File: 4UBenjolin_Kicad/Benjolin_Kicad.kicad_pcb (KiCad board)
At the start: 2 copper layers, 254 x 177.8 mm, 144 parts, among them J1 Conn_01x04_Male, J10 MAINOUT, J11 PWM, J12 RUN, J13 XOR, J14 CV_1, J15 CV_2, J16 Mix_In_3, J17 Mix_In_4, J18 Mixer_Out, J2 Mix_In_1, J3 Mix_In_2, J4 EXT.INPUT, J5 CV_F, J6 PUL2, J7 TRI1, J8 TRI2, J9 PUL1, Q1 BC547, SW1 SW_SPDT, U1 TL074, U2 TL072, U3 TL074, U4 TL074, U5 SSI2164, U6 4021, U7 L78L09_SOT89, U8 79L09, U9 TL071

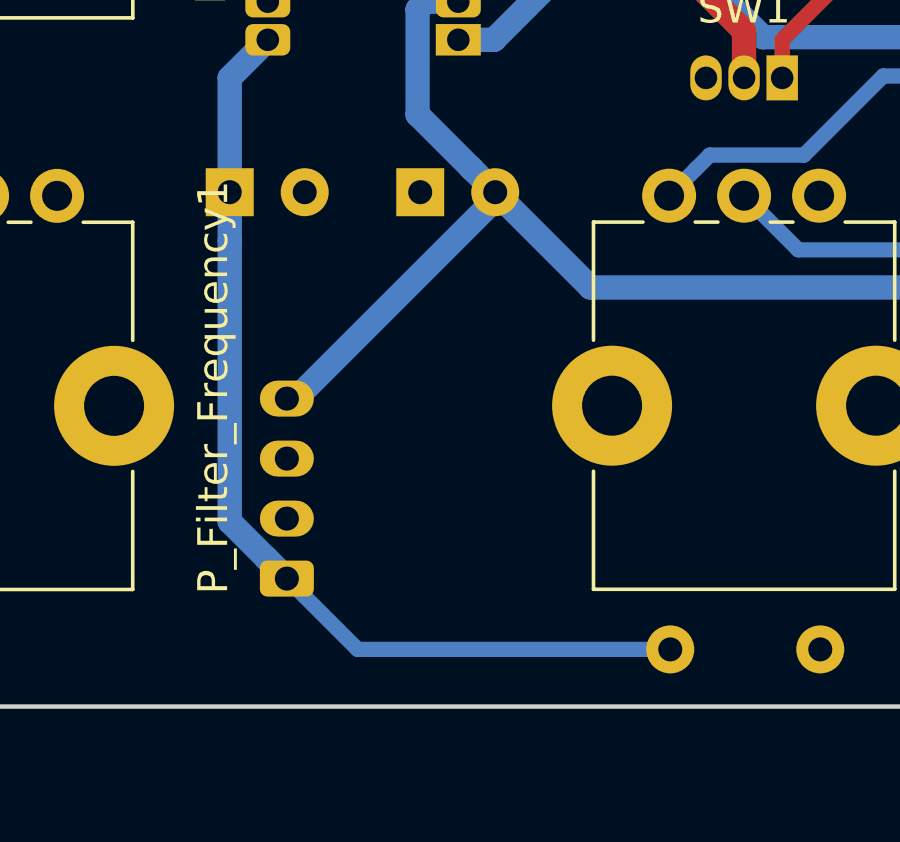
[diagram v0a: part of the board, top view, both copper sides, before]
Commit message: pots are off center still and need to connect one of the ground pins
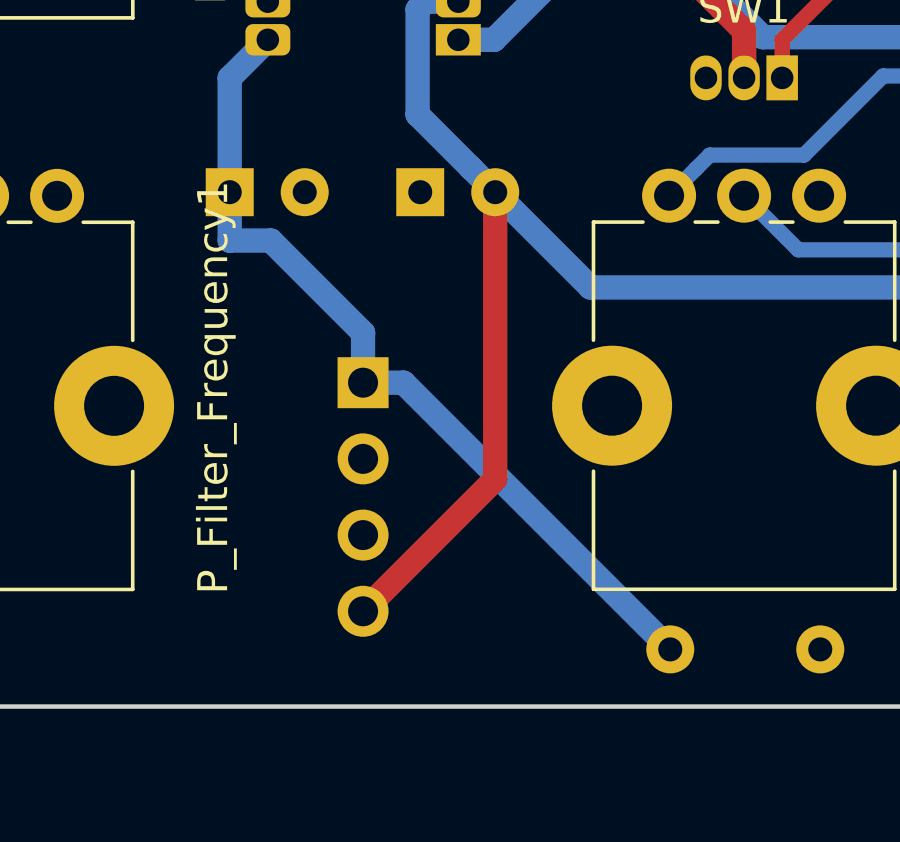
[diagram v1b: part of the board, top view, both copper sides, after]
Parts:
- J1: footprint Connector_Molex:Molex_Micro-Latch_53254-0470_1x04_P2.00mm_Horizontal -> Connector_PinHeader_2.54mm:PinHeader_1x04_P2.54mm_Vertical
- moved J1 7.01 mm to (254.0, 154.3), turned to 180 degrees
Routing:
- net -12V: track 37.7 -> 43.8 mm
- net +12V: track 33.0 -> 28.5 mm
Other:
- board text added: "Version 1"

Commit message: made separate panel
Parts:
- moved REF** 41.9 mm to (134.0, 71.4)
- moved REF** 41.9 mm to (134.0, 52.4)
- moved REF** 41.9 mm to (134.0, 90.5)
- moved REF** 41.9 mm to (134.0, 109.5)
- moved REF** 41.9 mm to (83.2, 52.4)
- moved REF** 41.9 mm to (83.2, 71.4)
- moved REF** 41.9 mm to (83.2, 90.5)
- moved REF** 41.9 mm to (83.2, 109.5)
- moved REF** 41.9 mm to (159.4, 52.4)
- moved REF** 41.9 mm to (159.4, 33.3)
- moved REF** 41.9 mm to (159.4, 71.4)
- moved REF** 41.9 mm to (108.6, 90.5)
- moved REF** 41.9 mm to (108.6, 71.4)
- moved REF** 41.9 mm to (108.6, 52.4)
- moved REF** 41.9 mm to (108.6, 109.5)
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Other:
- board size 254 x 177.8 mm -> 212.1 x 177.8 mm

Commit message: Built Gerbers
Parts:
- removed REF** (x17): Banana Jack, SynthComponents:Banana _Jack_Panel
- turned P_Chan1 to 270 degrees
- turned P_Chan2 to 270 degrees
- turned P_Chan3 to 270 degrees
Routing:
- net GND: track 22.3 -> 84.8 mm, vias 130 -> 146
- net Net-(J2-Pad1): track 18.7 -> 35.7 mm, vias 0 -> 1
- net Net-(J16-Pad1): track 20.6 -> 37.2 mm
- net Net-(P_Chan2-Pad2): track 10.3 -> 23.2 mm
- net Net-(P_Chan1-Pad2): track 36.8 -> 48.0 mm
- net Net-(P_Chan3-Pad2): track 9.63 -> 20.7 mm
- net Net-(J3-Pad1): track 26.8 -> 37.3 mm
- net FCV: track 34.9 -> 44.2 mm
- net Net-(C5-Pad1): track 186.2 -> 178.5 mm
- net V+: track 374.2 -> 370.3 mm, vias 10 -> 12
- net Net-(C19-Pad1): track 34.6 -> 36.3 mm
- net VCA1Out: track 84.3 -> 85.9 mm
- net Net-(J18-Pad1): track 41.8 -> 43.3 mm
- net RUN_CV: track 214.9 -> 213.4 mm, vias 7 -> 8
- net (no net): vias 2 -> 0
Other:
- board size 212.1 x 177.8 mm -> 101.6 x 152.4 mm
- board text removed: "4mm hole"
- board text removed: "BENJOLIN AND MIXER"
- board text removed: "CV"
- board text removed: "EXT. IN"
- board text removed: "FILTER FREQ"
- board text removed: "FREQ A"
- board text removed: "FREQ B"
- board text removed: "IN 1"
- board text removed: "IN 2"
- board text removed: "IN 3"
- board text removed: "IN 4"
- board text removed: "LOOP I/Ø"
- board text removed: "LOOP OFFSET"
- board text removed: "MAIN OUT"
- board text removed: "MIX OUT"
- board text removed: "PULSE"
- board text removed: "PWM"
- board text removed: "RESONANCE"
- board text removed: "RUNGLER"
- board text removed: "RUNGLER CV"
- board text removed: "TRIANGLE"
- board text removed: "XOR"

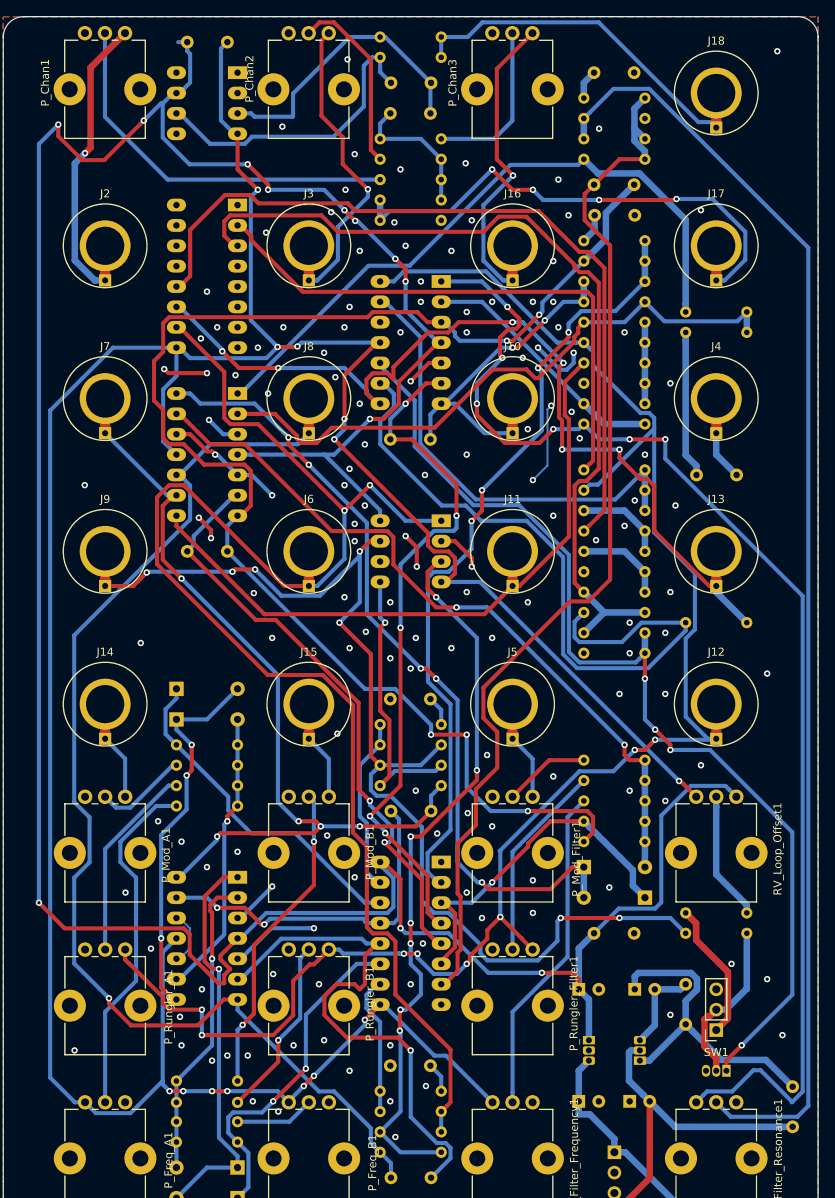
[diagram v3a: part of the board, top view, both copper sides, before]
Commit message: All bugs fixed. -v rail, flipped pots, power to 4021, tl071 opamp flipped
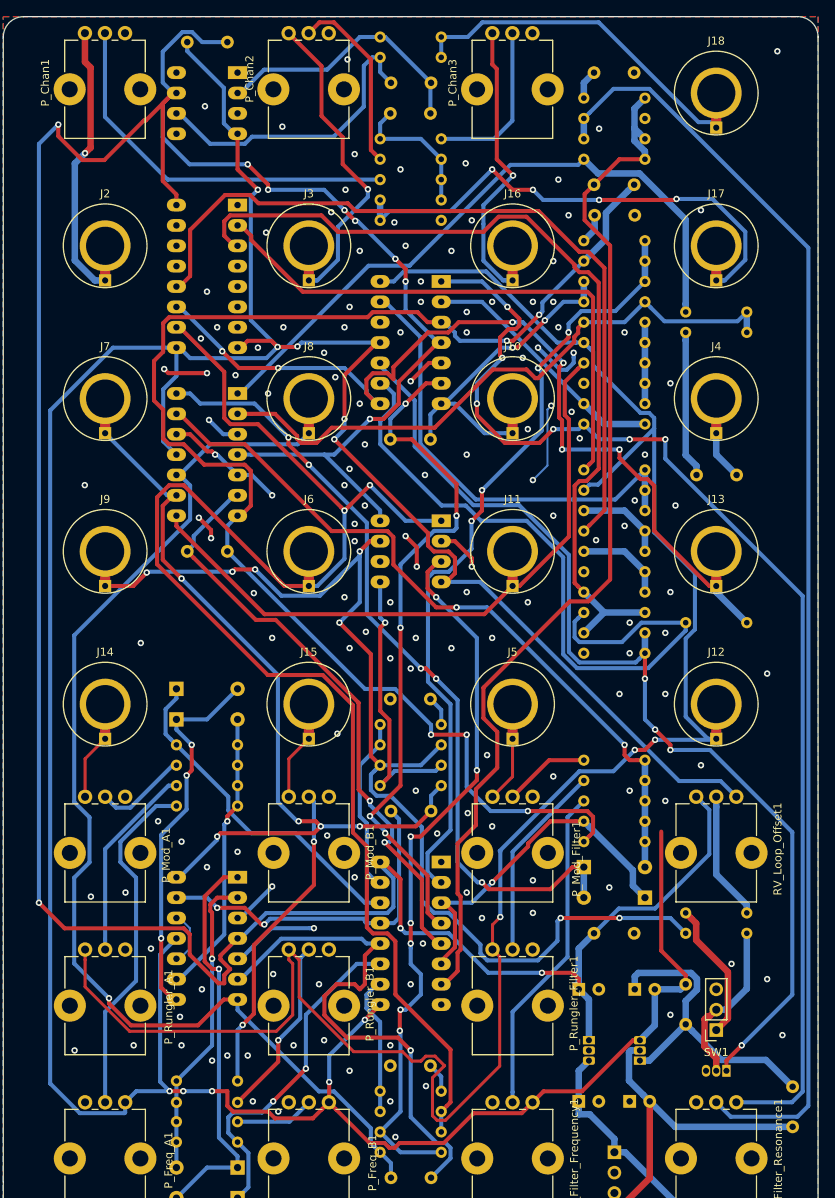
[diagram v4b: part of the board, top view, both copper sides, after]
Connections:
- C17 pad 2: Net-(C17-Pad2) -> V-
- C18 pad 2: Net-(C17-Pad2) -> V-
- C21 pad 1: V- -> V+
- C21 pad 2: V+ -> V-
- P_Chan1 pad 1: GND -> Net-(J2-Pad1)
- P_Chan1 pad 3: Net-(J2-Pad1) -> GND
- P_Chan2 pad 1: GND -> Net-(J3-Pad1)
- P_Chan2 pad 3: Net-(J3-Pad1) -> GND
- P_Chan3 pad 1: GND -> Net-(J16-Pad1)
- P_Chan3 pad 3: Net-(J16-Pad1) -> GND
- P_Filter_Frequency1 pad 1: V- -> GND
- P_Filter_Frequency1 pad 3: GND -> V-
- P_Filter_Resonance1 pad 1: P9R3B -> GND
- P_Filter_Resonance1 pad 3: GND -> P9R3B
- P_Freq_A1 pad 1: V- -> GND
- P_Freq_A1 pad 3: GND -> V-
- P_Freq_B1 pad 1: V- -> GND
- P_Freq_B1 pad 3: GND -> V-
- P_Mod_A1 pad 1: GND -> Net-(J14-Pad1)
- P_Mod_A1 pad 3: Net-(J14-Pad1) -> GND
- P_Mod_B1 pad 1: GND -> Net-(J15-Pad1)
- P_Mod_B1 pad 3: Net-(J15-Pad1) -> GND
- P_Mod_Filter1 pad 1: GND -> Net-(J5-Pad1)
- P_Mod_Filter1 pad 3: Net-(J5-Pad1) -> GND
- P_Rungler_A1 pad 1: GND -> RUN_CV
- P_Rungler_A1 pad 3: RUN_CV -> GND
- P_Rungler_B1 pad 1: GND -> RUN_CV
- P_Rungler_B1 pad 3: RUN_CV -> GND
- P_Rungler_Filter1 pad 1: GND -> RUN_CV
- P_Rungler_Filter1 pad 3: RUN_CV -> GND
- RV_Loop_Offset1 pad 1: V- -> V+
- RV_Loop_Offset1 pad 3: V+ -> V-
- U6 pad 16: Vdd -> V+
- U6 pad 8: Vss -> V-
- U8 pad 3: Net-(C17-Pad2) -> V-
- U9 pad 2: GND -> Net-(C19-Pad1)
- U9 pad 3: Net-(C19-Pad1) -> GND
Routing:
- net V-: track 358.7 -> 437.7 mm, vias 13 -> 10
- net RUN_CV: track 213.4 -> 249.4 mm, vias 8 -> 3
- net V+: track 370.3 -> 388.9 mm, vias 12 -> 11
- net Net-(C17-Pad2): track 11.2 -> 0.00 mm
- net P9R3B: track 158.9 -> 150.6 mm
- net Net-(C19-Pad1): track 36.3 -> 33.2 mm
- net Net-(J16-Pad1): track 37.2 -> 35.6 mm
- net Net-(J2-Pad1): track 35.7 -> 34.3 mm
- net Net-(J3-Pad1): track 37.3 -> 38.6 mm
- net GND: track 84.8 -> 84.9 mm, vias 146 -> 149
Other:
- board text added: "Version 2"
- board text removed: "Version 1"

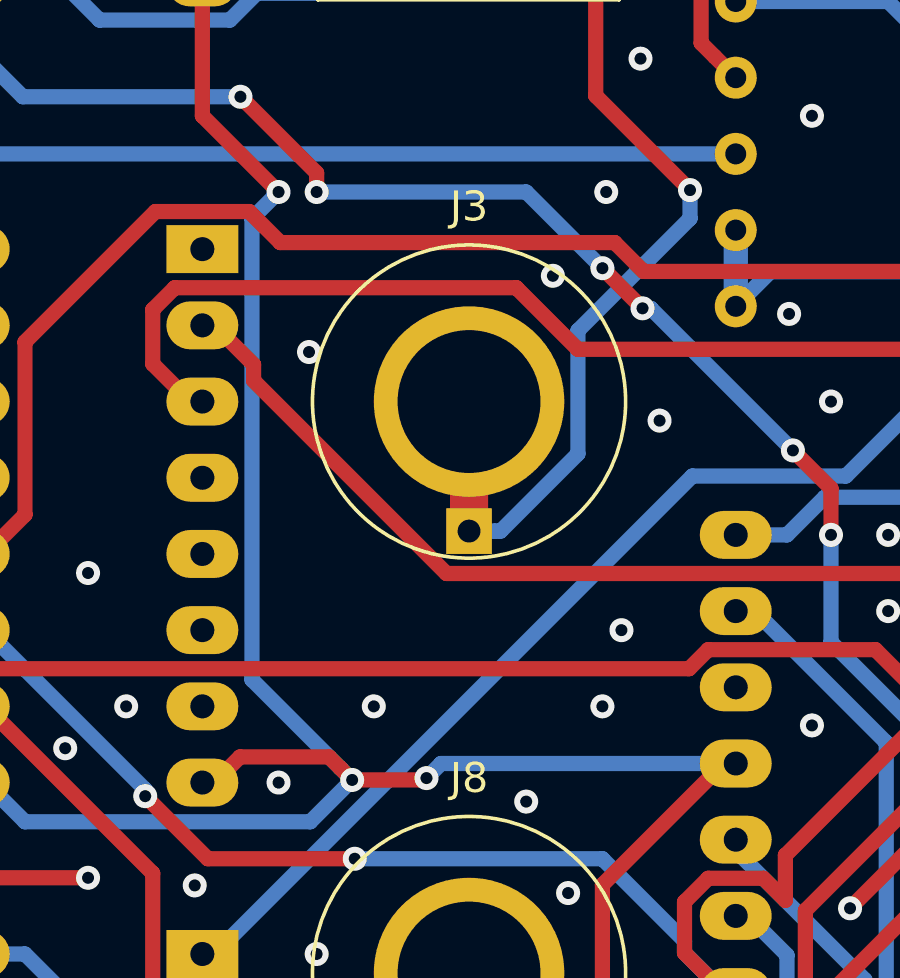
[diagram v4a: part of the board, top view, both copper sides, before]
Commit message: Renumbered the resistors. V2 built and sent to jlcpcb
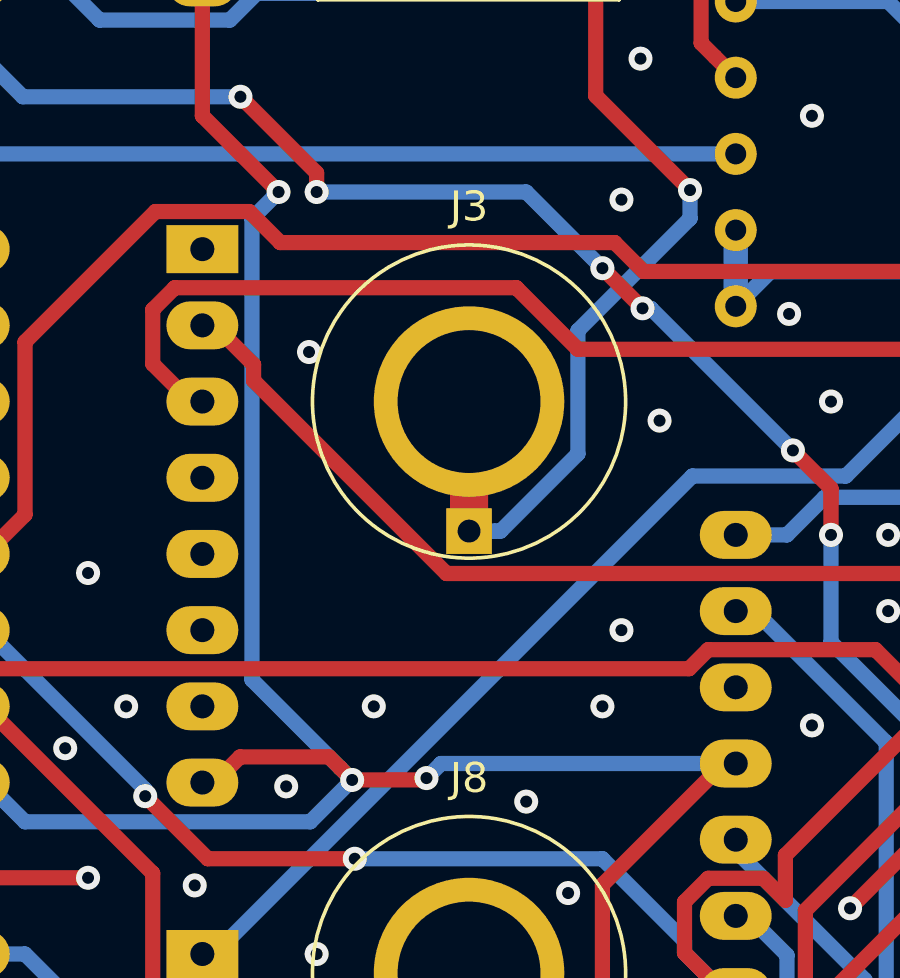
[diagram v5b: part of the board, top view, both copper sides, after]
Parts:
- renumbered R21 to R1, R46 to R10, R42 to R11, R50 to R12, R20 to R13, R18 to R14, R10 to R15, R11 to R16, R14 to R17, R31 to R18, R34 to R19, R17 to R2, R37 to R20, R49 to R21, R43 to R22, R38 to R23, R44 to R24, R45 to R25, R39 to R26, R15 to R27, R8 to R28, R16 to R29, R19 to R3, R28 to R30, R29 to R31, R30 to R32, R32 to R34, R56 to R35, R57 to R36, R55 to R37, R54 to R38, R53 to R39, R1 to R4, R52 to R40, R51 to R41, R23 to R42, R35 to R43, R47 to R44, R40 to R45, R24 to R46, R36 to R47, R41 to R49, R9 to R5, R12 to R50, R4 to R51, R3 to R52, R2 to R53, R7 to R54, R6 to R55, R5 to R56, R13 to R57, R25 to R6, R27 to R7, R26 to R8, R22 to R9
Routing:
- net GND: vias 149 -> 148
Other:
- board text added: "+12V"
- board text added: "-12V"
- board text added: "GND"
